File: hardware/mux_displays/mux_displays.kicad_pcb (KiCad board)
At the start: 2 copper layers, 35.3 x 47.5 mm, 17 parts, among them J1 Conn_01x05_Male, J2 Conn_01x05_Male, J3 Conn_01x02_Male, Q1 BC817, Q2 BC817, U1 KCSC02-123, U2 KCSC02-123

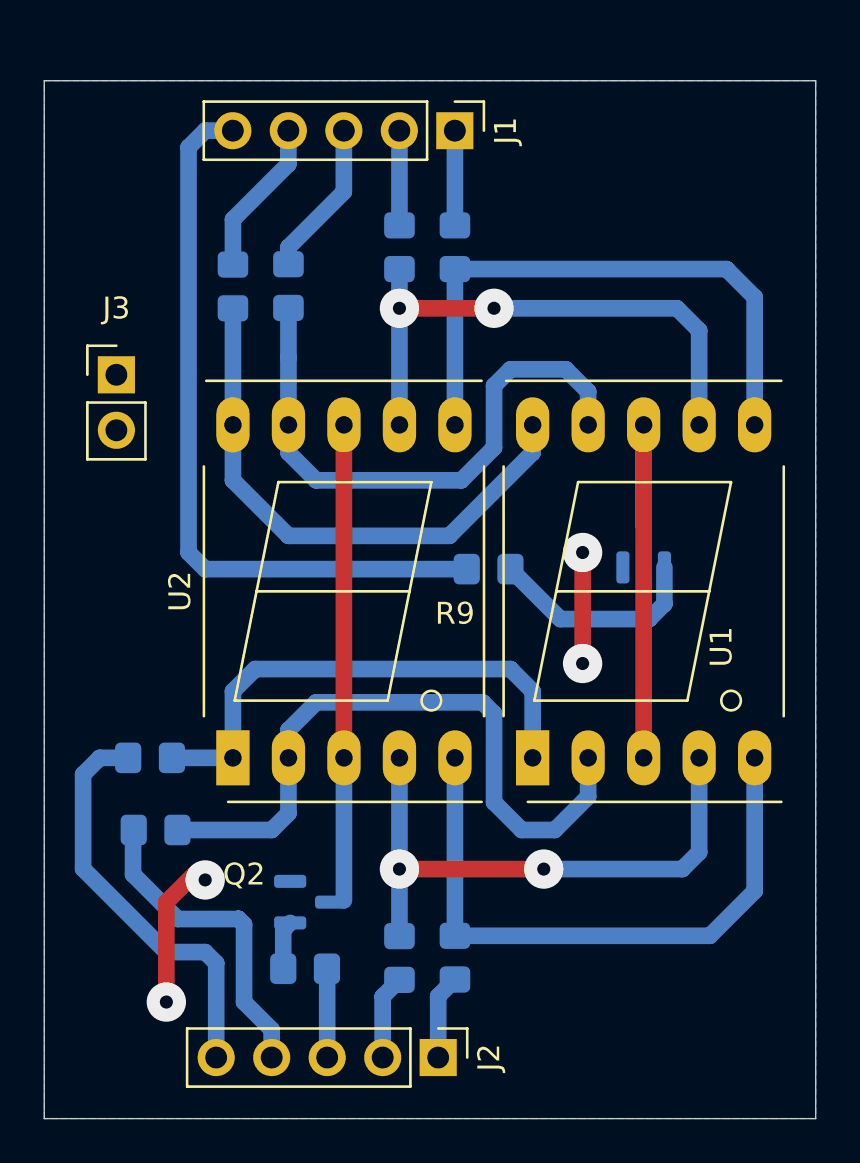
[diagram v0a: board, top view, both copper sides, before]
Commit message: Adicionado furos na placa de displays
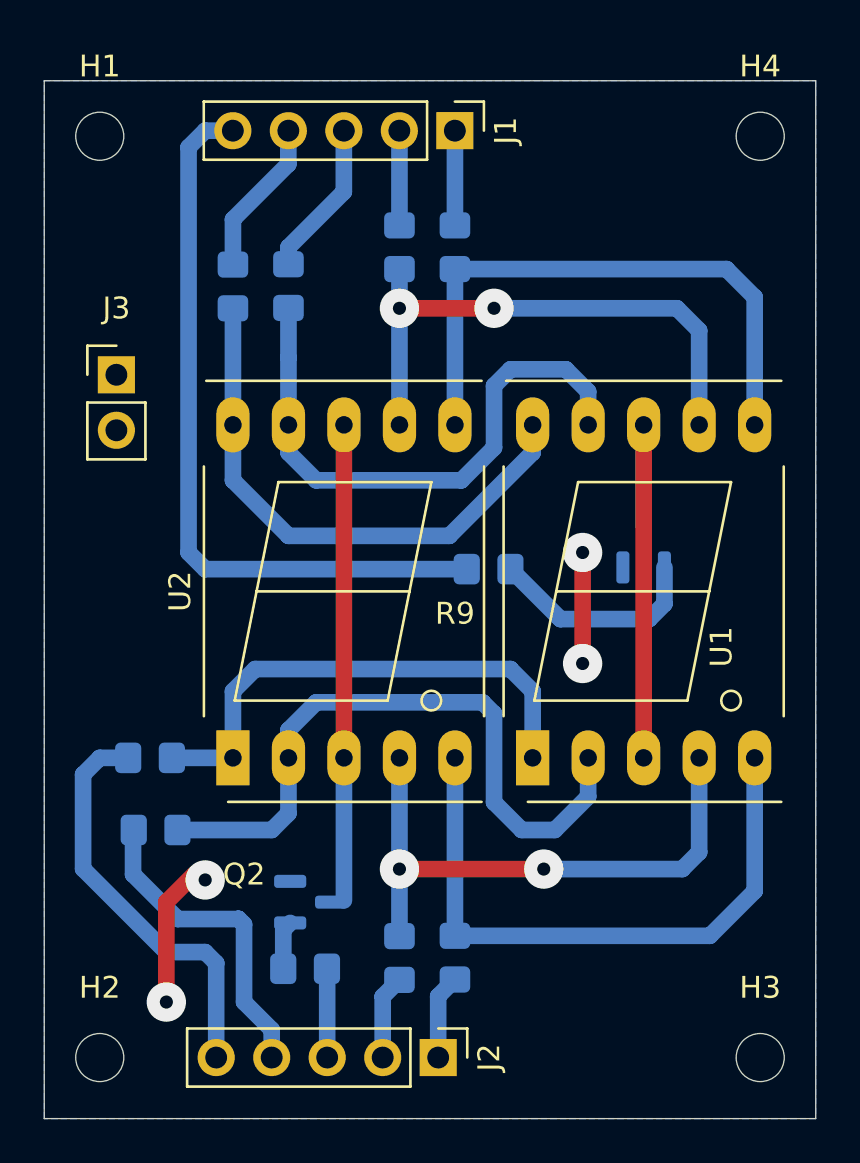
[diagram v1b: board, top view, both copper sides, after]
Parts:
- added H1: MountingHole, MountingHole:MountingHole_2.2mm_M2, F.Cu at (62.5, 45.2)
- added H2: MountingHole, MountingHole:MountingHole_2.2mm_M2, F.Cu at (62.5, 87.4)
- added H3: MountingHole, MountingHole:MountingHole_2.2mm_M2, F.Cu at (92.7, 87.4)
- added H4: MountingHole, MountingHole:MountingHole_2.2mm_M2, F.Cu at (92.7, 45.2)
- R18, R9: value 330 -> 2k2
